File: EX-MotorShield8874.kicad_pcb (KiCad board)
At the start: 4 copper layers, 68.6 x 53.3 mm, 101 parts, among them J1 Power, J11 I2C, J12 OLED, J13 MC 1,5/ 2-G-3,5, J14 STEMMA QT, J15 MC 1,5/ 2-G-3,5, J2 Digital/PWM, J3 Analog, J4 Digital/PWM, J51 Barrel_Jack_MountingPin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

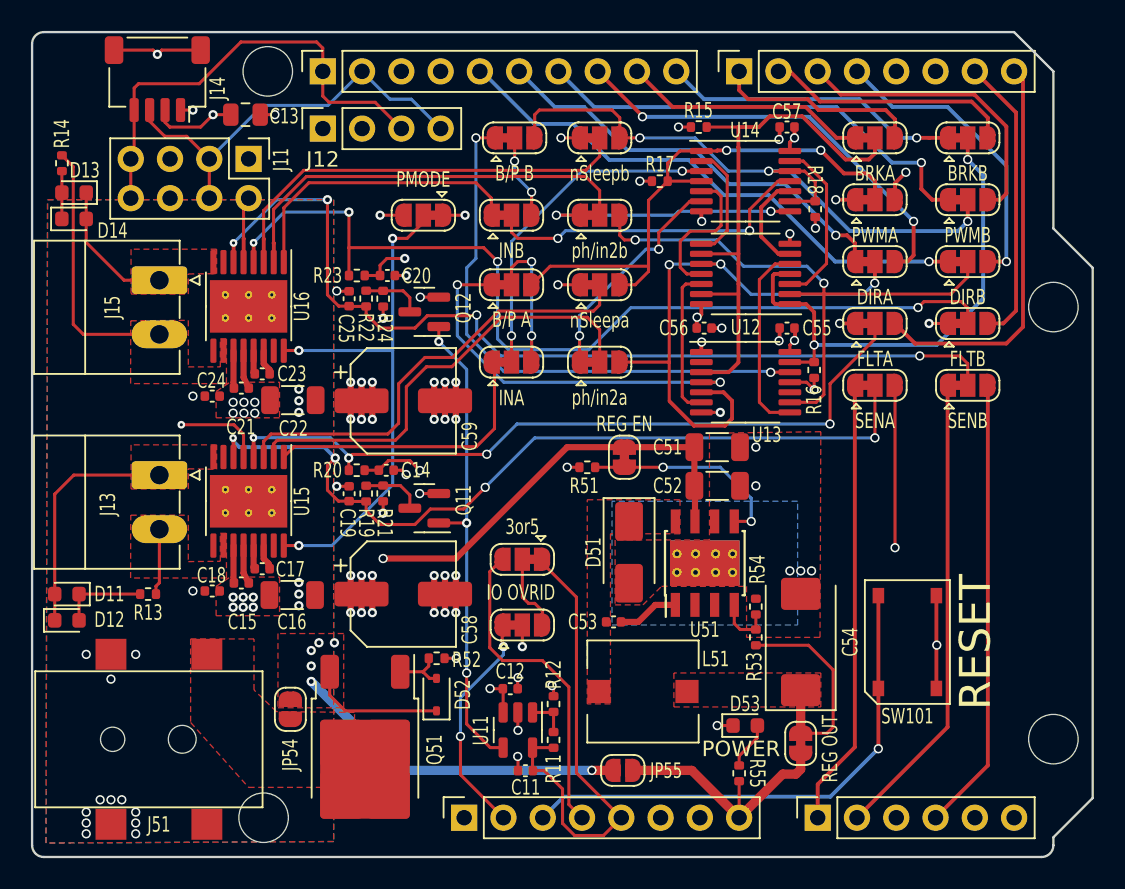
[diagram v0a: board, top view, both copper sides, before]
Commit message: Trace/via size consistency, better defaults, minor trace cleanup.
1) Set up Net Classes with default trace and via sizes.

2) Set all traces/vias to consistent sizes based on NetClass.

3) Minor trace re-routing based on the changes above.

4) Added a documentation block on pours and priorities.

Checked DRC again.
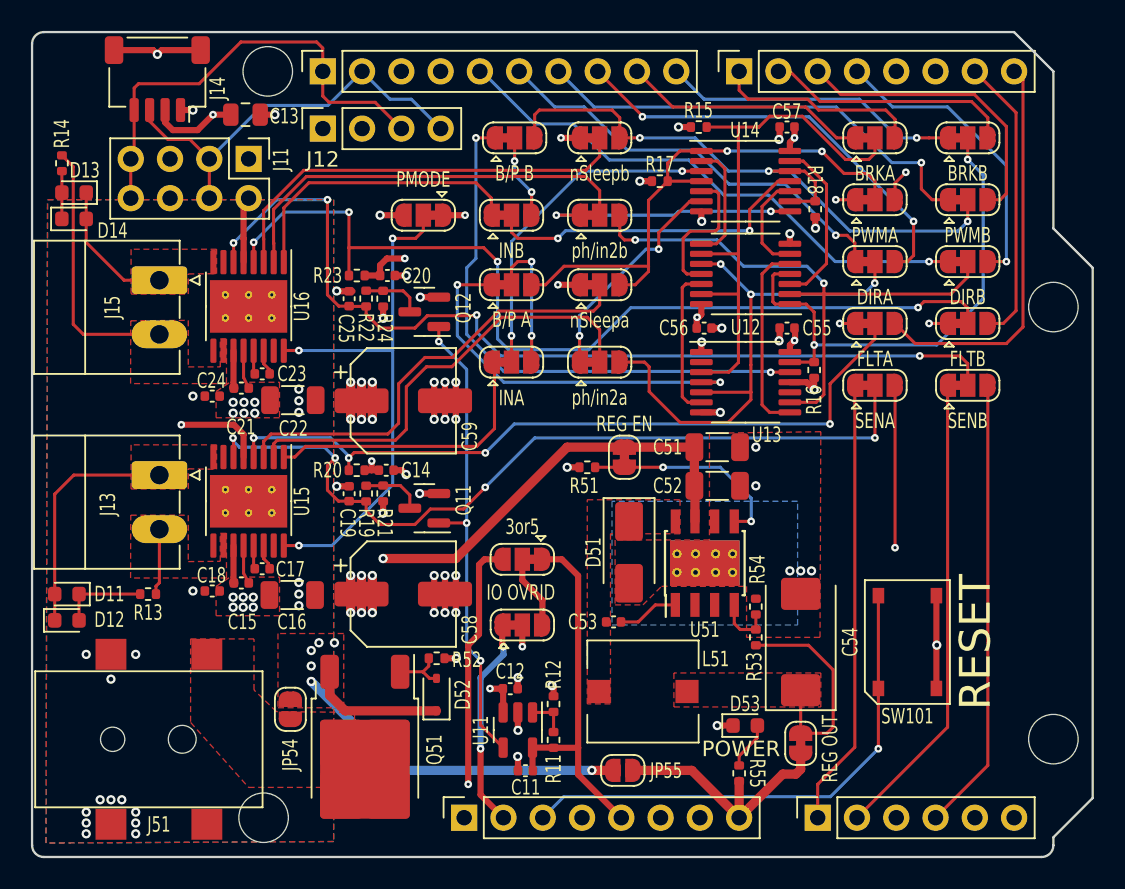
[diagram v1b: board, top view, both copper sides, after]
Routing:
- net +5V: track 30.9 -> 24.0 mm
- net +3V3: track 110.4 -> 104.5 mm, vias 1 -> 2
- net VBUS: track 61.7 -> 58.0 mm
- net /direction_a: track 37.4 -> 35.4 mm
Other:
- board text added: "Layer Utilization F.Cu - Primary Signal Traces: - Pour driver-thermal-ground, Net GND, Priority 0 - Pour ph, Net ph, Priority 8 - Pour converter-thermal-top, Net GND, Priority 9 - Pour v_conn, Net v_conn, Priority 12 - Pour Vdrive, Net Vdrive, Priority 20 - Signal traces. - All components. In1.Cu - Ground Plane - Pour ground, Net GND, Priority 3. In2.Cu - Power Planes: - Pour Vdrive, Net Vdrive, 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"

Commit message: First attempt at making the A or B pinout "one jumper" configurable.
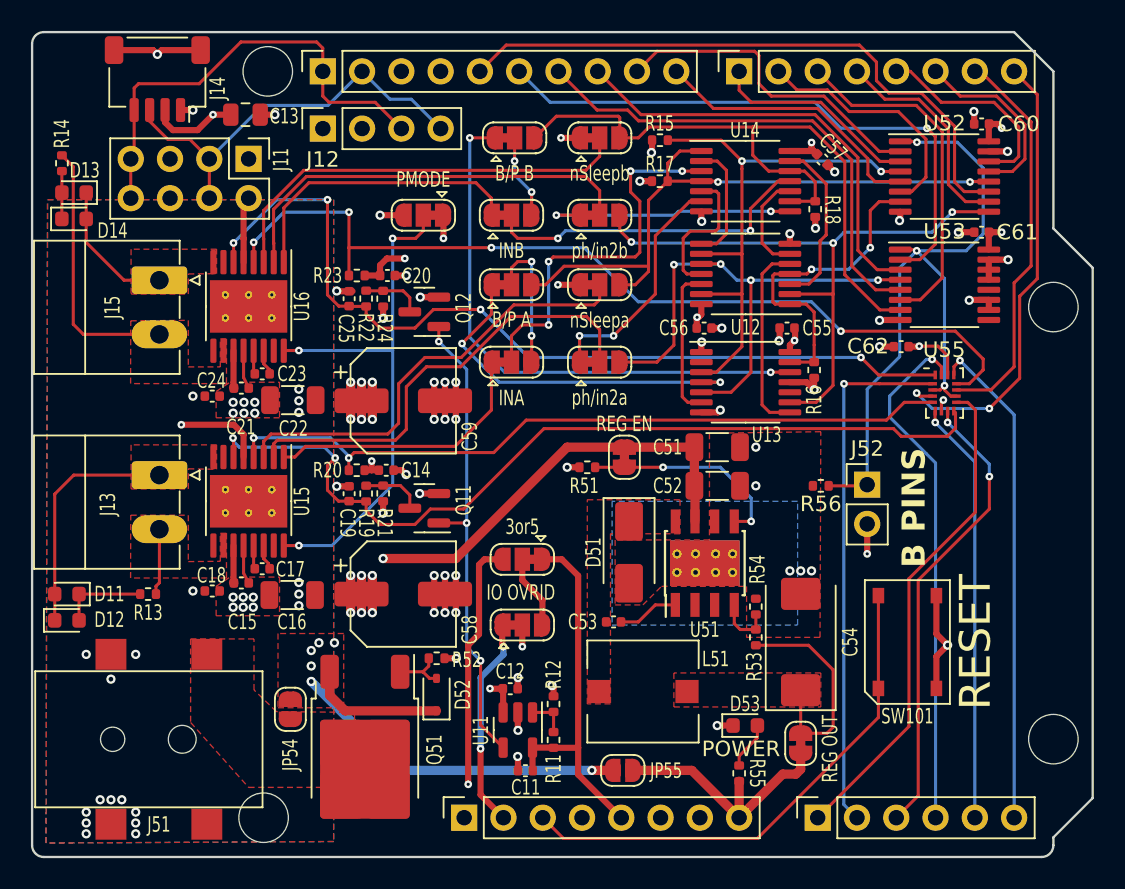
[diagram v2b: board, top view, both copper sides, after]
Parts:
- removed JP11: PWMA, Jumper:SolderJumper-3_P1.3mm_Bridged12_RoundedPad1.0x1.5mm
- removed JP12: BRKA, Jumper:SolderJumper-3_P1.3mm_Bridged12_RoundedPad1.0x1.5mm
- removed JP13: PWMB, Jumper:SolderJumper-3_P1.3mm_Bridged12_RoundedPad1.0x1.5mm
- removed JP14: BRKB, Jumper:SolderJumper-3_P1.3mm_Bridged12_RoundedPad1.0x1.5mm
- removed JP15: DIRB, Jumper:SolderJumper-3_P1.3mm_Bridged12_RoundedPad1.0x1.5mm
- removed JP16: DIRA, Jumper:SolderJumper-3_P1.3mm_Bridged12_RoundedPad1.0x1.5mm
- removed JP17: FLTA, Jumper:SolderJumper-3_P1.3mm_Bridged12_RoundedPad1.0x1.5mm
- removed JP18: FLTB, Jumper:SolderJumper-3_P1.3mm_Bridged12_RoundedPad1.0x1.5mm
- removed JP19: SENB, Jumper:SolderJumper-3_P1.3mm_Bridged12_RoundedPad1.0x1.5mm
- removed JP20: SENA, Jumper:SolderJumper-3_P1.3mm_Bridged12_RoundedPad1.0x1.5mm
- added C60: 100nF, Capacitor_SMD:C_0402_1005Metric, F.Cu at (161.4, 52.6)
- added C61: 100nF, Capacitor_SMD:C_0402_1005Metric, F.Cu at (161.4, 59.6)
- added C62: 100nF, Capacitor_SMD:C_0402_1005Metric, F.Cu at (156.2, 67.0)
- added J52: A or B, Connector_PinHeader_2.54mm:PinHeader_1x02_P2.54mm_Vertical, F.Cu at (154.0, 75.9)
- added R56: 47K, Resistor_SMD:R_0402_1005Metric, F.Cu at (151.0, 76.0)
- added U52: 74HC157, Package_SO:TSSOP-16_4.4x5mm_P0.65mm, F.Cu at (159.0, 56.0)
- added U53: 74HC157, Package_SO:TSSOP-16_4.4x5mm_P0.65mm, F.Cu at (159.0, 63.0)
- added U55: FSA2466, DCC-EX-Footprints:UQFN-16_2.1x2.9_Pitch0.4mm, F.Cu at (159.0, 70.0)
- moved C57 3.10 mm to (151.1, 54.9), turned to -45 degrees
- moved R15 2.65 mm to (140.6, 53.6)
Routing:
- net /a_or_b: track 0.00 -> 46.7 mm, vias 0 -> 3
- net /brake_b: track 33.6 -> 21.1 mm
- net GND: track 53.2 -> 64.9 mm, vias 68 -> 77
- net VBUS: track 58.0 -> 69.2 mm, vias 13 -> 17
- net /def_direction_a: track 27.5 -> 38.3 mm
- net /def_fault_n_a: track 36.6 -> 27.4 mm
- net /alt_fault_n_b: track 18.7 -> 25.6 mm
- net /alt_direction_b: track 19.6 -> 14.1 mm, vias 1 -> 0
- net /def_brake_a: track 15.9 -> 21.3 mm
- net /pwm_a: track 35.7 -> 41.1 mm
- net /def_direction_b: track 35.3 -> 40.3 mm, vias 1 -> 0
- net /alt_sen_b: track 29.4 -> 33.6 mm, vias 0 -> 1
- net /alt_fault_n_a: track 26.0 -> 29.9 mm, vias 0 -> 2
- net /def_sen_b: track 30.4 -> 34.1 mm, vias 0 -> 1
- net /sen_a: track 53.2 -> 56.8 mm, vias 4 -> 2
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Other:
- board text added: "B PINS"
